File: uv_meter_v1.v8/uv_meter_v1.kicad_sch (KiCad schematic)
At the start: 47 parts, among them J101 CONN_DC_PWR_JACK, J401 SD, J501 VH, SW101 SK-12F17-G, SW601 BUTTON_PTS64, U101 3.3V, 200mA, U102 3.3V, 200mA, U103 5V, 200mA, U201 Socket STM32, U301 LMV358, U501 MCP2562

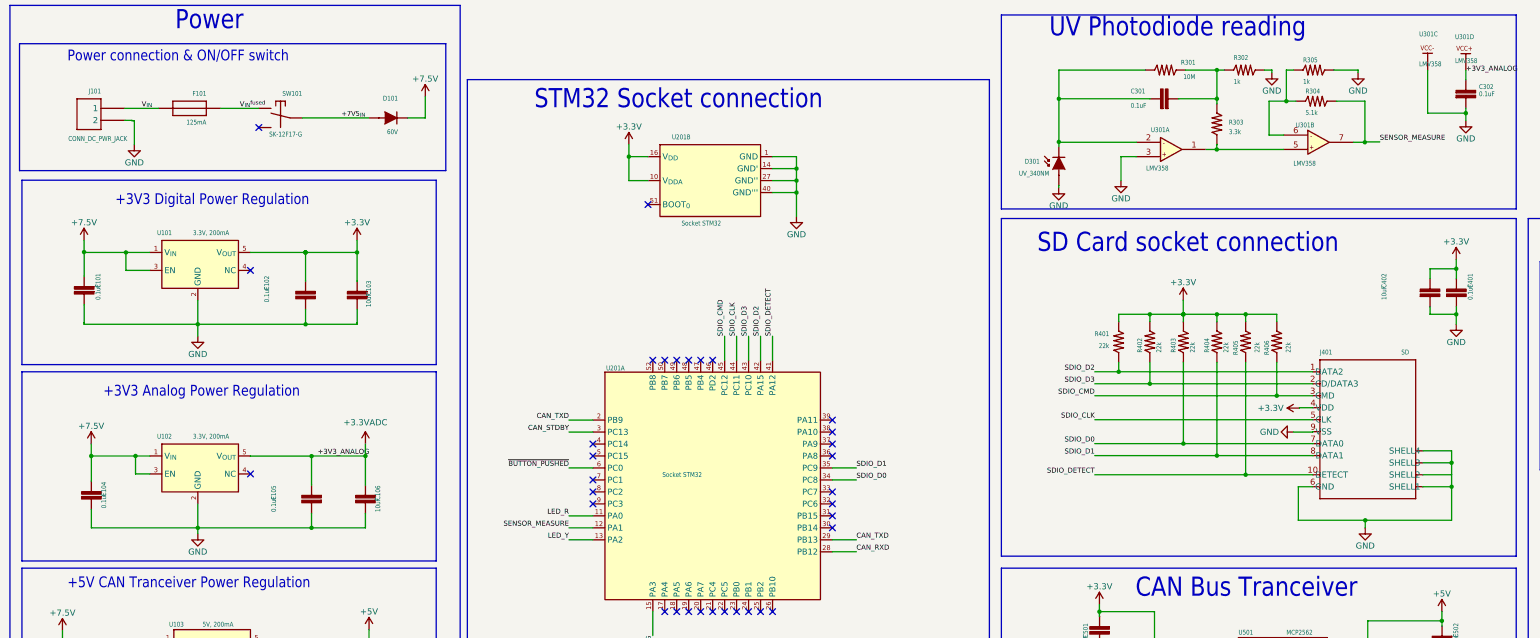
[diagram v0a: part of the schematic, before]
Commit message: Update power jack and SD card connector in schematic
* Update components according to their library counterparts :
  - SD Card connector
  - DC power jack
* Update schematic to fix disrepencies due to components updates
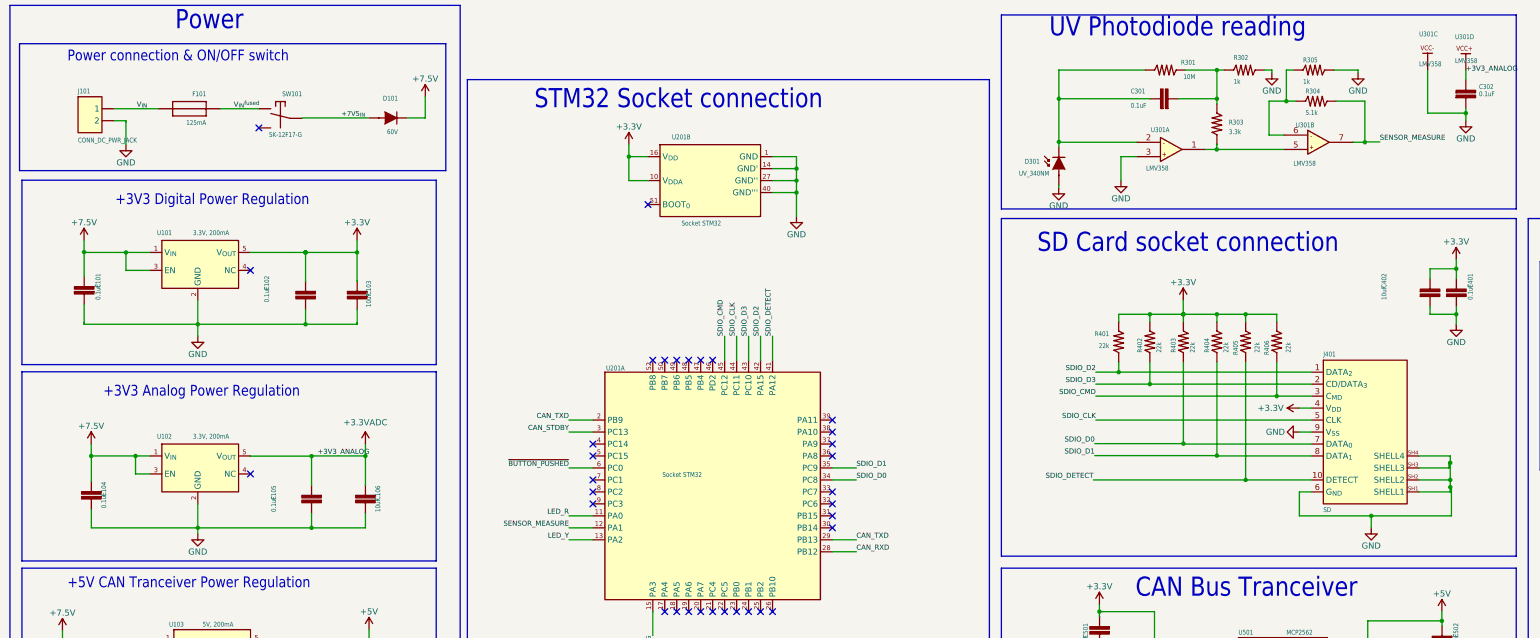
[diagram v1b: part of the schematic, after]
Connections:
- net +7V5_{IN}: no longer SW101.IN

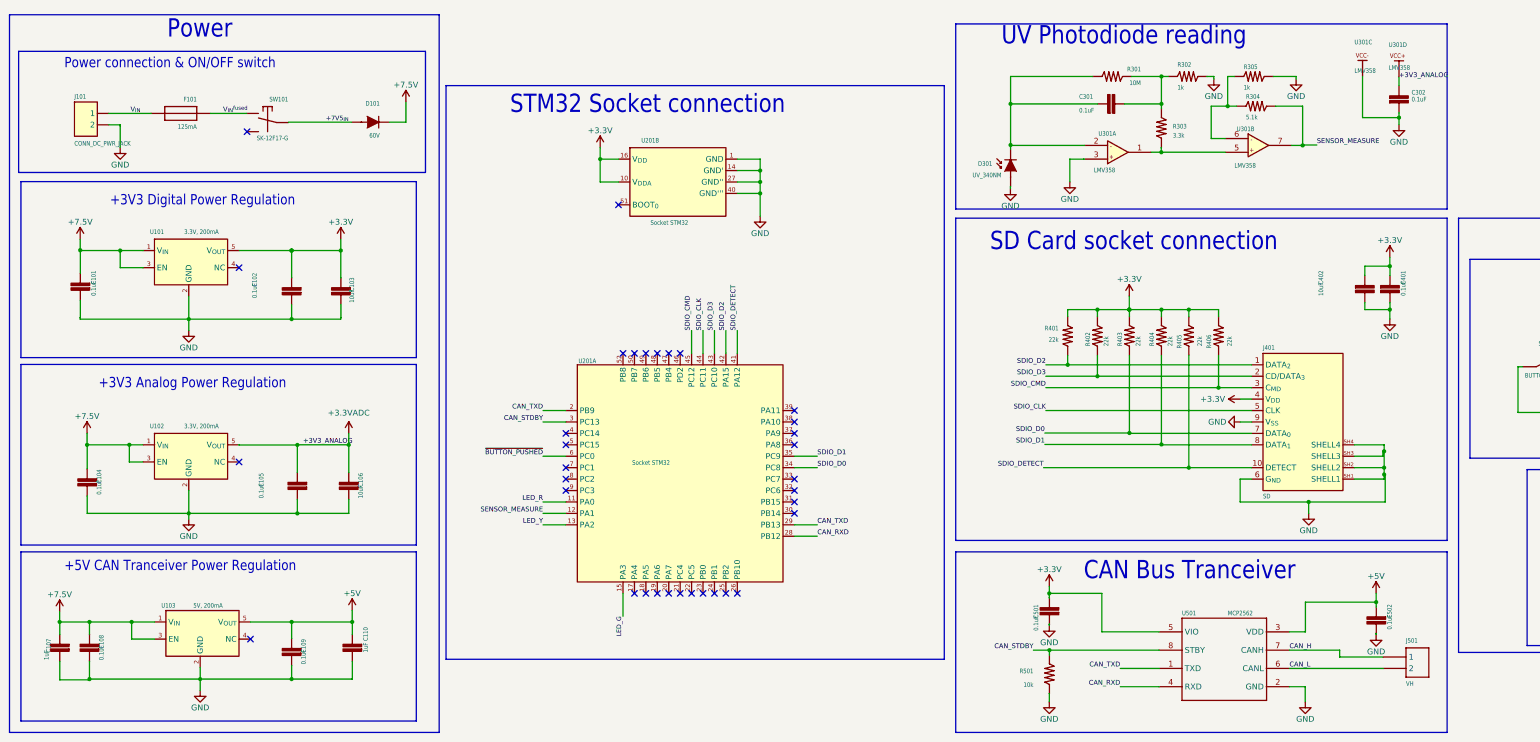
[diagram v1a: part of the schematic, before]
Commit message: Update some capacitors and resistors
* Update schematic with 100nF capacitors from library.
* Update schematic with 1k resistor from library.
* All updated components now fit schematic grid.
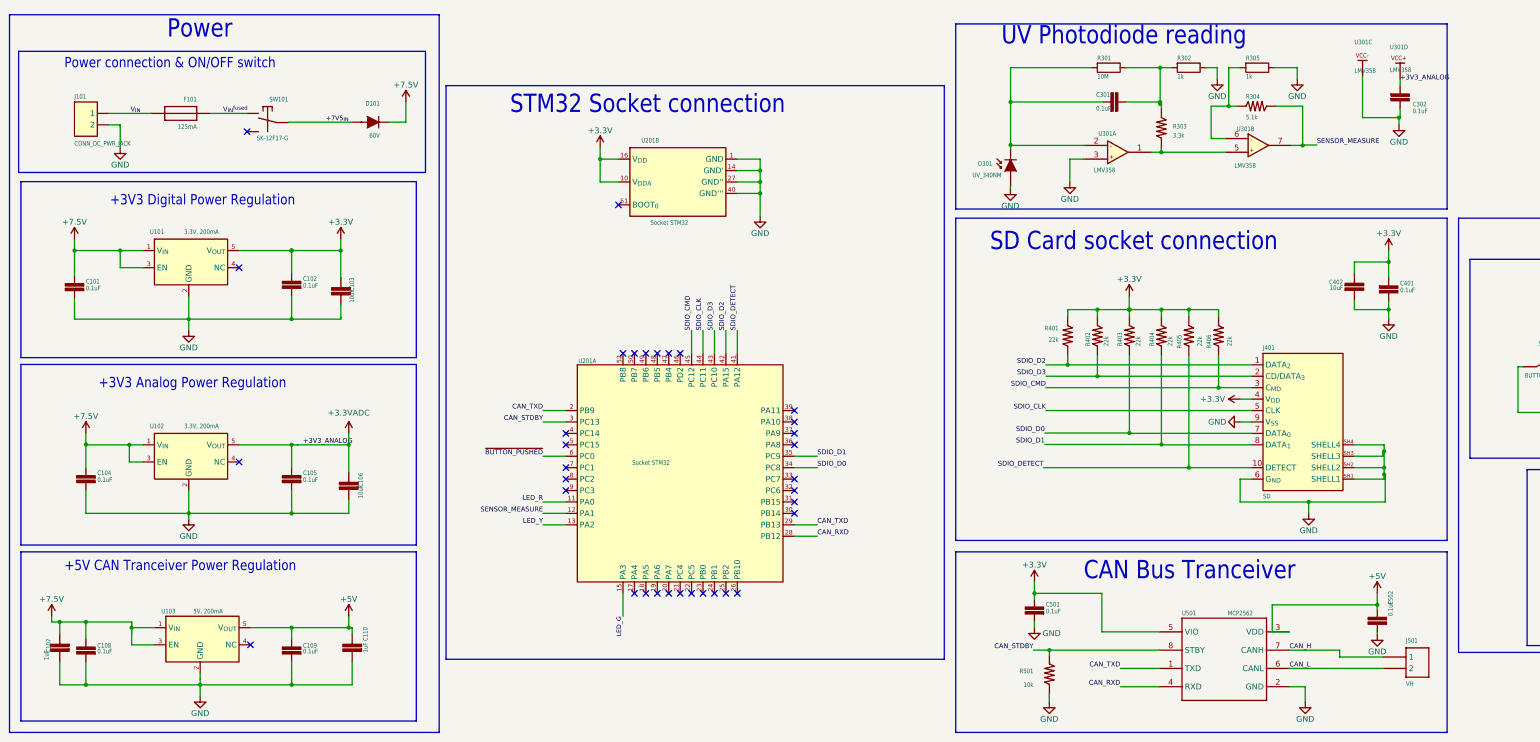
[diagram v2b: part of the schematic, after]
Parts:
- C101, C102, C104, C105, C108, C109, C301, C302, C401, C501, C502: symbol uv_meter_v1-eagle-import:0.1UF -> uv_meter_v1-eagle-import:100nF
- R301: symbol uv_meter_v1-eagle-import:10MOHM -> uv_meter_v1-eagle-import:10MΩ; Panasonic's Surface mount resistors technical guide (Vers. 3) (none) -> https://industrial.panasonic.com/cdbs/www-data/pdf/RDA0000/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; Product catalog (none) -> https://industrial.panasonic.com/cdbs/www-data/pdf/RDA0000/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; Recommended Soldering Conditions (none) -> https://industrial.panasonic.com/cdbs/www-data/pdf/RDA0000/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; Recommended land pattern (none) -> https://industrial.panasonic.com/cdbs/www-data/pdf/RDA0000/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
- R302, R305: symbol uv_meter_v1-eagle-import:1KOHM -> uv_meter_v1-eagle-import:1kΩ
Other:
- moved on the sheet: C101, C102, C104, C105, C108, C301, C402, C501, U103, U301D
